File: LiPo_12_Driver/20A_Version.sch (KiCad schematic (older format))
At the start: 47 parts

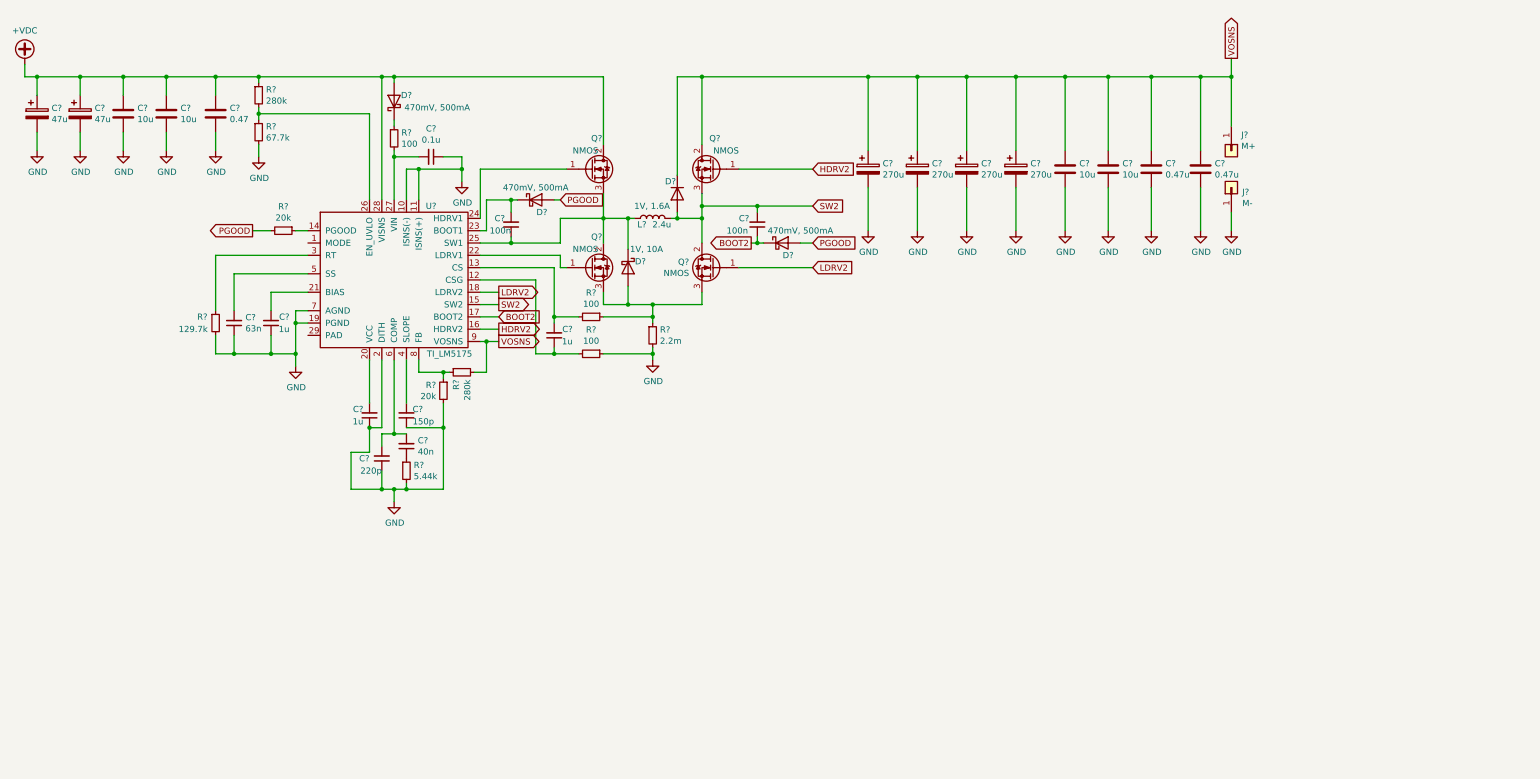
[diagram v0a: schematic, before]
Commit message: Finished LIPO Schematic, started PCB design
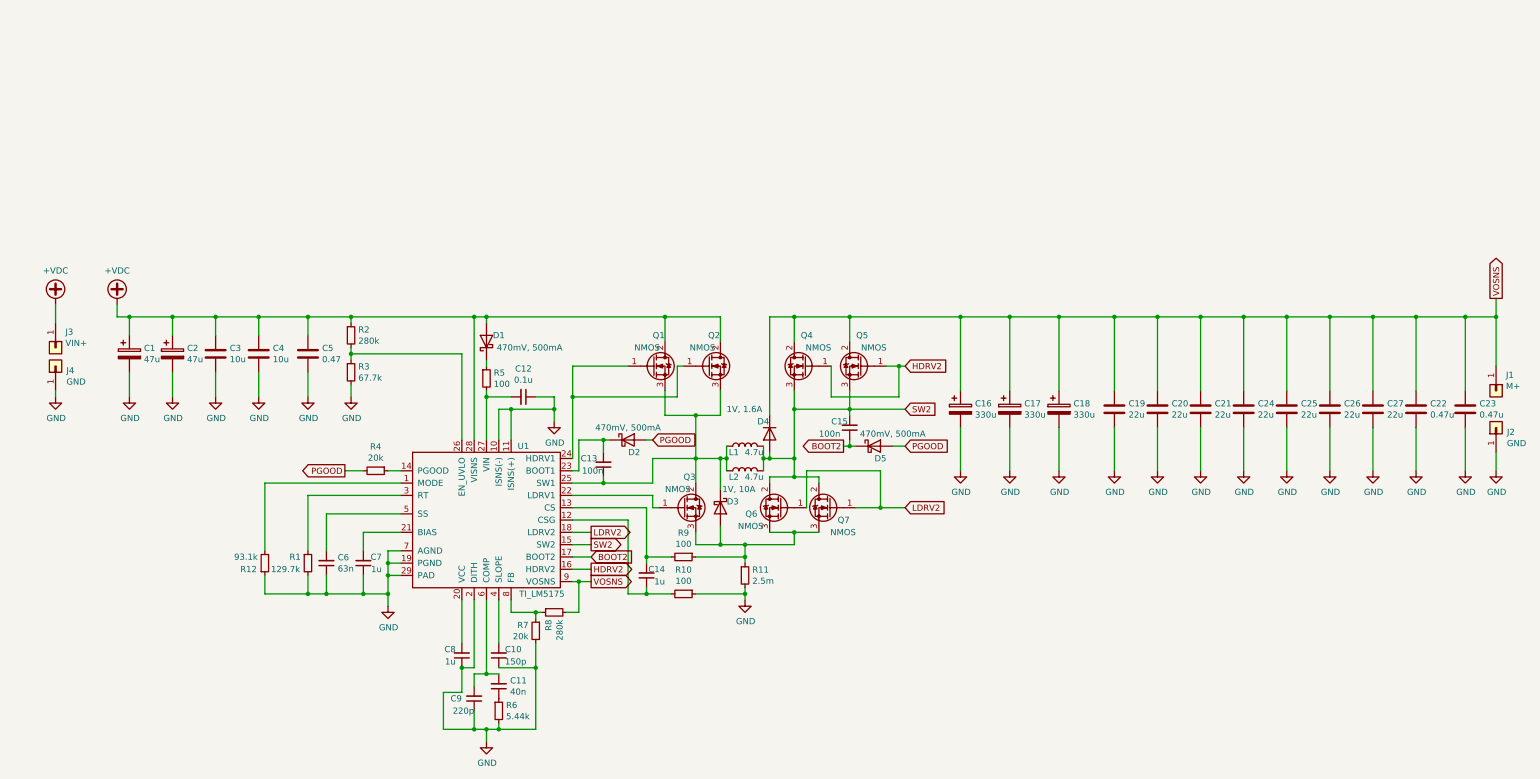
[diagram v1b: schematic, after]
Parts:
- removed C?: 270u, symbol Device:CP
- added C19, C24, C25, C26, C27: 22u, Capacitor_SMD:C_1210_3225Metric_Pad1.42x2.65mm_HandSolder, symbol Device:C
- added J3: VIN+, Connector_PinHeader_2.54mm:PinHeader_1x01_P2.54mm_Vertical, symbol Connector_Generic:Conn_01x01
- added J4: GND, Connector_PinHeader_2.54mm:PinHeader_1x01_P2.54mm_Vertical, symbol Connector_Generic:Conn_01x01
- added L2: 4.7u, Inductor_SMD:L_Vishay_IHLP-6767, symbol Device:L
- added Q2: NMOS, Package_SON:VSONP-8-1EP_5x6_P1.27mm, symbol Device:Q_NMOS_GDS
- added Q4, Q6: NMOS, Package_SON:VSON-8_3.3x3.3mm_P0.65mm_NexFET, symbol Device:Q_NMOS_GDS
- added R12: 93.1k, Resistor_SMD:R_0603_1608Metric_Pad1.05x0.95mm_HandSolder, symbol Device:R_Small
- C1, C2: renamed from C?; footprint (none) -> Capacitor_SMD:CP_Elec_6.3x7.7
- C10, C11, C12, C13, C22, C23, C5, C6, C9: renamed from C?; footprint (none) -> Capacitor_SMD:C_0603_1608Metric_Pad1.05x0.95mm_HandSolder
- C14, C15, C7, C8: renamed from C?; footprint (none) -> Capacitor_SMD:C_0805_2012Metric_Pad1.15x1.40mm_HandSolder
- C16, C17, C18: renamed from C?; value 270u -> 330u; footprint (none) -> Capacitor_SMD:CP_Elec_6.3x9.9
- C20, C21: renamed from C?; value 10u -> 22u; footprint (none) -> Capacitor_SMD:C_1210_3225Metric_Pad1.42x2.65mm_HandSolder
- C3, C4: renamed from C?; footprint (none) -> Capacitor_SMD:C_1210_3225Metric_Pad1.42x2.65mm_HandSolder
- D1, D2, D5: renamed from D?; footprint (none) -> Diode_SMD:D_SOD-123
- D3: renamed from D?; footprint (none) -> Package_TO_SOT_SMD:TO-252-2
- D4: renamed from D?; footprint (none) -> Diode_SMD:D_SMA_Handsoldering
- J1: renamed from J?; footprint (none) -> Connector_PinHeader_2.54mm:PinHeader_1x01_P2.54mm_Vertical
- J2: renamed from J?; value M- -> GND; footprint (none) -> Connector_PinHeader_2.54mm:PinHeader_1x01_P2.54mm_Vertical
- L1: renamed from L?; value 2.4u -> 4.7u; footprint (none) -> Inductor_SMD:L_Vishay_IHLP-6767
- Q1, Q3: renamed from Q?; footprint (none) -> Package_SON:VSONP-8-1EP_5x6_P1.27mm
- Q5, Q7: renamed from Q?; footprint (none) -> Package_SON:VSON-8_3.3x3.3mm_P0.65mm_NexFET
- R1, R2, R3, R6: renamed from R?; footprint (none) -> Resistor_SMD:R_0402_1005Metric
- R10, R4, R5, R7, R8, R9: renamed from R?; footprint (none) -> Resistor_SMD:R_0603_1608Metric_Pad1.05x0.95mm_HandSolder
- R11: renamed from R?; value 2.2m -> 2.5m; footprint (none) -> Resistor_SMD:R_2816_7142Metric_Pad3.20x4.45mm_HandSolder
- U1: renamed from U?; footprint (none) -> Package_DFN_QFN:QFN-28-1EP_4x5mm_P0.5mm_EP2.65x3.65mm_ThermalVias
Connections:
- net +VDC: now also J3.1 (Pin_1), Q2.2 (D)
- net GND: now also U1.29 (PAD), C19.2, C24.2, C25.2, C26.2, C27.2, J4.1 (Pin_1), R12.1
- net HDRV2: now also Q4.1 (G)
- net LDRV2: now also Q6.1 (G)
- net SW2: now also L2.2, Q4.3 (S), Q6.2 (D)
- net VOSNS: now also C19.1, C24.1, C25.1, C26.1, C27.1, Q4.2 (D)
- net at C13.1, D3.1 (K), L1.1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: now also L2.1, Q2.3 (S)
- net at U1.1 (MODE): now also R12.2
- net at Q1.1 (G), U1.24 (HDRV1): now also Q2.1 (G)
- net at D3.2 (A), Q3.3 (S), Q7.3 (S)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: now also Q6.3 (S)
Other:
- moved on the sheet: C1, C10, C11, C12, C13, C14, C15, C16, C17, C18, C2, C20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

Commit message: more lipo pcb dev
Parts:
- removed Q1, Q2, Q3: NMOS, Package_SON:VSONP-8-1EP_5x6_P1.27mm, symbol Device:Q_NMOS_GDS
- removed Q4, Q5, Q6, Q7: NMOS, Package_SON:VSON-8_3.3x3.3mm_P0.65mm_NexFET, symbol Device:Q_NMOS_GDS
- added Q1, Q2, Q3: Q_NMOS, Package_SON:VSONP-8-1EP_5x6_P1.27mm, symbol Device:Q_NMOS_SGD
- added Q4, Q5, Q6, Q7: Q_NMOS, Package_SON:VSON-8_3.3x3.3mm_P0.65mm_NexFET, symbol Device:Q_NMOS_SGD
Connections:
- net +VDC: now also Q1.3 (D), Q2.3 (D)
- net HDRV2: now also Q4.2 (G), Q5.2 (G)
- net LDRV2: now also Q6.2 (G), Q7.2 (G)
- net SW2: now also Q4.1 (S), Q5.1 (S), Q6.3 (D), Q7.3 (D)
- net VOSNS: now also Q4.3 (D), Q5.3 (D)
- net at C13.1, D3.1 (K), L1.1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: now also Q1.1 (S), Q2.1 (S), Q3.3 (D)
- net at U1.22 (LDRV1): now also Q3.2 (G)
- net at U1.24 (HDRV1): now also Q1.2 (G), Q2.2 (G)
- net at D3.2 (A), R11.1, R9.1: now also Q3.1 (S), Q6.1 (S), Q7.1 (S)
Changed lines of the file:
@@
 Wire Wire Line
 	3650 5400 3800 5400
-$Comp
-L Device:Q_NMOS_GDS Q3
-U 1 1 617B6E80
-P 6400 5700
-F 0 "Q3" H 6400 5950 50  0000 L CNN
-F 1 "NMOS" H 6250 5850 50  0000 L CNN
-F 2 "Package_SON:VSONP-8-1EP_5x6_P1.27mm" H 6600 5800 50  0001 C CNN
-F 3 "~" H 6400 5700 50  0001 C CNN
-	1    6400 5700
-	1    0    0    -1
-$EndComp
-$Comp
-L Device:Q_NMOS_GDS Q1
-U 1 1 617B7257
-P 6150 4550
-F 0 "Q1" H 6150 4800 50  0000 L CNN
-F 1 "NMOS" H 6000 4700 50  0000 L CNN
-F 2 "Package_SON:VSONP-8-1EP_5x6_P1.27mm" H 6350 4650 50  0001 C CNN
-F 3 "~" H 6150 4550 50  0001 C CNN
-	1    6150 4550
-	1    0    0    -1
-$EndComp
-$Comp
-L Device:Q_NMOS_GDS Q5
-U 1 1 617B7625
-P 7850 4550
-F 0 "Q5" H 7800 4800 50  0000 L CNN
-F 1 "NMOS" H 7650 4700 50  0000 L CNN
-F 2 "Package_SON:VSON-8_3.3x3.3mm_P0.65mm_NexFET" H 8050 4650 50  0001 C CNN
-F 3 "~" H 7850 4550 50  0001 C CNN
-	1    7850 4550
-	-1   0    0    -1
-$EndComp
-$Comp
-L Device:Q_NMOS_GDS Q7
-U 1 1 617B7A51
-P 7600 5700
-F 0 "Q7" H 7450 5600 50  0000 L CNN
-F 1 "NMOS" H 7400 5500 50  0000 L CNN
-F 2 "Package_SON:VSON-8_3.3x3.3mm_P0.65mm_NexFET" H 7800 5800 50  0001 C CNN
-F 3 "~" H 7600 5700 50  0001 C CNN
-	1    7600 5700
-	-1   0    0    -1
-$EndComp
 Wire Wire Line
 	6750 5300 6700 5300
@@
 Wire Wire Line
 	6250 4950 6250 4750
-$Comp
-L Device:Q_NMOS_GDS Q2
-U 1 1 618E7504
+Wire Wire Line
+	6700 4750 6700 4950
+Wire Wire Line
+	6700 4950 6500 4950
+Connection ~ 6500 4950
+Wire Wire Line
+	6700 4350 6700 4150
+Wire Wire Line
+	6700 4150 6250 4150
+Connection ~ 6250 4150
+Wire Wire Line
+	5500 4800 6350 4800
+Wire Wire Line
+	6350 4800 6350 4550
+Wire Wire Line
+	6350 4550 6400 4550
+Connection ~ 5500 4800
+Wire Wire Line
+	5500 4800 5500 4550
+Wire Wire Line
+	7300 4900 7300 5300
+Wire Wire Line
+	7100 5300 7300 5300
+Connection ~ 7100 5300
+Connection ~ 7300 5300
+Wire Wire Line
+	7300 5300 7300 5450
+Wire Wire Line
+	7800 5700 8000 5700
+Wire Wire Line
+	7500 5900 7300 5900
+Wire Wire Line
+	7100 5900 7300 5900
+Connection ~ 7300 5900
+Wire Wire Line
+	7100 5500 7100 5450
+Wire Wire Line
+	7100 5450 7300 5450
+Connection ~ 7300 5450
+Wire Wire Line
+	7500 5500 7500 5450
+Wire Wire Line
+	7500 5450 7300 5450
+Wire Wire Line
+	8000 5700 8000 5400
+Wire Wire Line
+	8000 5400 7400 5400
+Wire Wire Line
+	7400 5400 7400 5700
+Connection ~ 8000 5700
+Wire Wire Line
+	8000 5700 8200 5700
+Wire Wire Line
+	7750 4150 7750 4350
+Connection ~ 7750 4150
+Wire Wire Line
+	7750 4150 8650 4150
+Wire Wire Line
+	7750 4750 7750 4900
+Wire Wire Line
+	8050 4550 8150 4550
+Wire Wire Line
+	8150 4550 8150 4800
+Wire Wire Line
+	8150 4800 7600 4800
+Wire Wire Line
+	7600 4800 7600 4550
+Connection ~ 8150 4550
+Wire Wire Line
+	8150 4550 8200 4550
+$Comp
+L Device:Q_NMOS_SGD Q1
+U 1 1 617B93BB
+P 6150 4550
+F 0 "Q1" H 6100 4800 50  0000 L CNN
+F 1 "Q_NMOS" H 5900 4700 50  0000 L CNN
+F 2 "Package_SON:VSONP-8-1EP_5x6_P1.27mm" H 6350 4650 50  0001 C CNN
+F 3 "~" H 6150 4550 50  0001 C CNN
+	1    6150 4550
+	1    0    0    -1
+$EndComp
+$Comp
+L Device:Q_NMOS_SGD Q2
+U 1 1 617BFAC8
 P 6600 4550
 F 0 "Q2" H 6600 4800 50  0000 L CNN
-F 1 "NMOS" H 6450 4700 50  0000 L CNN
+F 1 "Q_NMOS" H 6350 4700 50  0000 L CNN
 F 2 "Package_SON:VSONP-8-1EP_5x6_P1.27mm" H 6800 4650 50  0001 C CNN
 F 3 "~" H 6600 4550 50  0001 C CNN
@@
 	1    0    0    -1
 $EndComp
-Wire Wire Line
-	6700 4750 6700 4950
-Wire Wire Line
-	6700 4950 6500 4950
-Connection ~ 6500 4950
-Wire Wire Line
-	6700 4350 6700 4150
-Wire Wire Line
-	6700 4150 6250 4150
-Connection ~ 6250 4150
-Wire Wire Line
-	5500 4800 6350 4800
-Wire Wire Line
-	6350 4800 6350 4550
-Wire Wire Line
-	6350 4550 6400 4550
-Connection ~ 5500 4800
-Wire Wire Line
-	5500 4800 5500 4550
-Wire Wire Line
-	7300 4900 7300 5300
-Wire Wire Line
-	7100 5300 7300 5300
-Connection ~ 7100 5300
-Connection ~ 7300 5300
-Wire Wire Line
-	7300 5300 7300 5450
-$Comp
-L Device:Q_NMOS_GDS Q6
-U 1 1 61939310
+$Comp
+L Device:Q_NMOS_SGD Q3
+U 1 1 617C90DC
+P 6400 5700
+F 0 "Q3" H 6400 5950 50  0000 L CNN
+F 1 "Q_NMOS" H 6150 5850 50  0000 L CNN
+F 2 "Package_SON:VSONP-8-1EP_5x6_P1.27mm" H 6600 5800 50  0001 C CNN
+F 3 "~" H 6400 5700 50  0001 C CNN
+	1    6400 5700
+	1    0    0    -1
+$EndComp
+$Comp
+L Device:Q_NMOS_SGD Q4
+U 1 1 617CFEE4
+P 7400 4550
+F 0 "Q4" H 7400 4800 50  0000 L CNN
+F 1 "Q_NMOS" H 7100 4700 50  0000 L CNN
+F 2 "Package_SON:VSON-8_3.3x3.3mm_P0.65mm_NexFET" H 7600 4650 50  0001 C CNN
+F 3 "~" H 7400 4550 50  0001 C CNN
+	1    7400 4550
+	-1   0    0    -1
+$EndComp
+$Comp
+L Device:Q_NMOS_SGD Q5
+U 1 1 617D5AFF
+P 7850 4550
+F 0 "Q5" H 7850 4800 50  0000 L CNN
+F 1 "Q_NMOS" H 7550 4700 50  0000 L CNN
+F 2 "Package_SON:VSON-8_3.3x3.3mm_P0.65mm_NexFET" H 8050 4650 50  0001 C CNN
+F 3 "~" H 7850 4550 50  0001 C CNN
+	1    7850 4550
+	-1   0    0    -1
+$EndComp
+$Comp
+L Device:Q_NMOS_SGD Q6
+U 1 1 617D7412
 P 7200 5700
-F 0 "Q6" H 7400 5650 50  0000 L CNN
-F 1 "NMOS" H 7350 5550 50  0000 L CNN
+F 0 "Q6" H 7050 5750 50  0000 L CNN
+F 1 "Q_NMOS" H 6950 5900 50  0000 L CNN
 F 2 "Package_SON:VSON-8_3.3x3.3mm_P0.65mm_NexFET" H 7400 5800 50  0001 C CNN
 F 3 "~" H 7200 5700 50  0001 C CNN
@@
 	-1   0    0    -1
 $EndComp
-Wire Wire Line
-	7800 5700 8000 5700
-Wire Wire Line
-	7500 5900 7300 5900
-Wire Wire Line
-	7100 5900 7300 5900
-Connection ~ 7300 5900
-Wire Wire Line
-	7100 5500 7100 5450
-Wire Wire Line
-	7100 5450 7300 5450
-Connection ~ 7300 5450
-Wire Wire Line
-	7500 5500 7500 5450
-Wire Wire Line
-	7500 5450 7300 5450
-Wire Wire Line
-	8000 5700 8000 5400
-Wire Wire Line
-	8000 5400 7400 5400
-Wire Wire Line
-	7400 5400 7400 5700
-Connection ~ 8000 5700
-Wire Wire Line
-	8000 5700 8200 5700
-$Comp
-L Device:Q_NMOS_GDS Q4
-U 1 1 61982AE0
-P 7400 4550
-F 0 "Q4" H 7350 4800 50  0000 L CNN
-F 1 "NMOS" H 7200 4700 50  0000 L CNN
-F 2 "Package_SON:VSON-8_3.3x3.3mm_P0.65mm_NexFET" H 7600 4650 50  0001 C CNN
-F 3 "~" H 7400 4550 50  0001 C CNN
-	1    7400 4550
+$Comp
+L Device:Q_NMOS_SGD Q7
+U 1 1 617D87B0
+P 7600 5700
+F 0 "Q7" H 7500 5850 50  0000 L CNN
+F 1 "Q_NMOS" H 7250 5750 50  0000 L CNN
+F 2 "Package_SON:VSON-8_3.3x3.3mm_P0.65mm_NexFET" H 7800 5800 50  0001 C CNN
+F 3 "~" H 7600 5700 50  0001 C CNN
+	1    7600 5700
 	-1   0    0    -1
 $EndComp
-Wire Wire Line
-	7750 4150 7750 4350
-Connection ~ 7750 4150
-Wire Wire Line
-	7750 4150 8650 4150
-Wire Wire Line
-	7750 4750 7750 4900
-Wire Wire Line
-	8050 4550 8150 4550
-Wire Wire Line
-	8150 4550 8150 4800
-Wire Wire Line
-	8150 4800 7600 4800
-Wire Wire Line
-	7600 4800 7600 4550
-Connection ~ 8150 4550
-Wire Wire Line
-	8150 4550 8200 4550
 $EndSCHEMATC

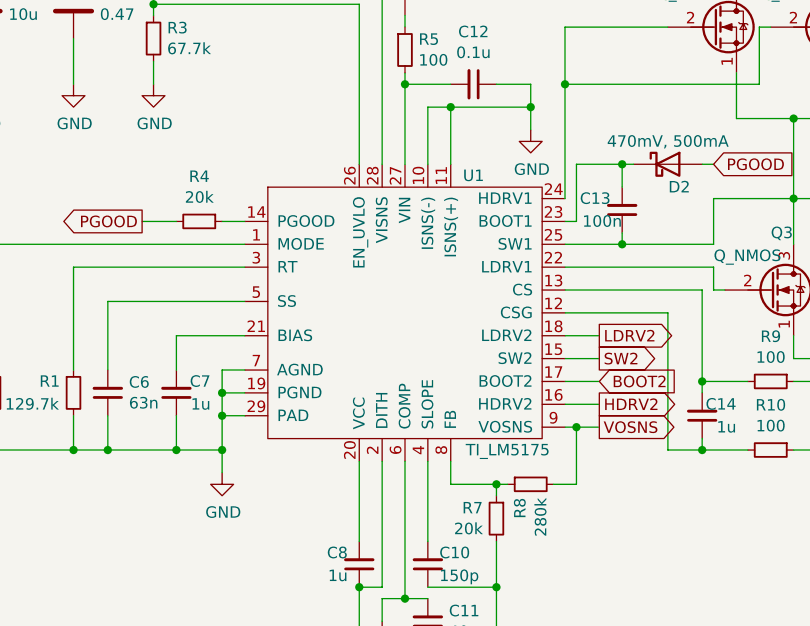
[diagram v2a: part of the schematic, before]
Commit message: Updated PCB because QFN package is out of stockaslhdflsakghlksa
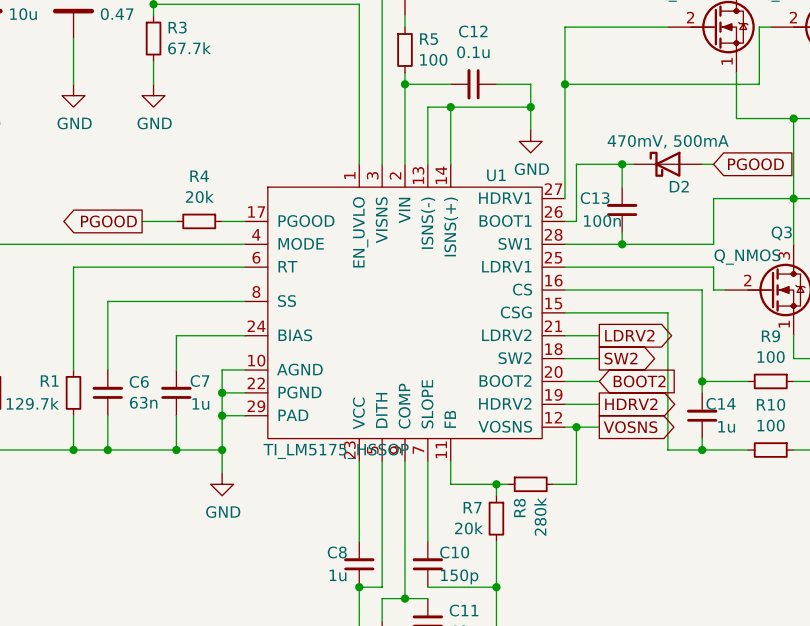
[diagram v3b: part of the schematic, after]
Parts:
- removed U1: TI_LM5175, Package_DFN_QFN:QFN-28-1EP_4x5mm_P0.5mm_EP2.65x3.65mm_ThermalVias, symbol LiPo_12_Driver:TI_LM5175
- added U1: TI_LM5175_HSSOP, Package_SO:HTSSOP-28-1EP_4.4x9.7mm_P0.65mm_EP3.4x9.5mm_ThermalVias, symbol LiPo_12_Driver:TI_LM5175_HSSOP
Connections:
- net +VDC: now also U1.3 (VISNS)
- net BOOT2: now also U1.20 (BOOT2)
- net GND: now also U1.10 (AGND), U1.13 (ISNS(-)), U1.14 (ISNS(+)), U1.22 (PGND), U1.29 (PAD), U1.5 (DITH)
- net HDRV2: now also U1.19 (HDRV2)
- net LDRV2: now also U1.21 (LDRV2)
- net SW2: now also U1.18 (SW2)
- net VOSNS: now also U1.12 (VOSNS)
- net at C13.1, D3.1 (K), L1.1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: now also U1.28 (SW1)
- net at R12.2: now also U1.4 (MODE)
- net at C14.1, R10.2: now also U1.15 (CSG)
- net at C14.2, R9.2: now also U1.16 (CS)
- net at R4.1: now also U1.17 (PGOOD)
- net at C8.2: now also U1.23 (VCC)
- net at C7.2: now also U1.24 (BIAS)
- net at Q3.2 (G): now also U1.25 (LDRV1)
- net at C13.2, D2.1 (K): now also U1.26 (BOOT1)
- net at Q1.2 (G), Q2.2 (G): now also U1.27 (HDRV1)
- net at R2.2, R3.1: now also U1.1 (EN_UVLO)
- net at C12.2, R5.2: now also U1.2 (VIN)
- net at R1.1: now also U1.6 (RT)
- net at C10.2: now also U1.7 (SLOPE)
- net at C6.2: now also U1.8 (SS)
- net at C11.2, C9.2: now also U1.9 (COMP)
- net at R7.1, R8.1: now also U1.11 (FB)
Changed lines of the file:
@@
 Wire Wire Line
 	3500 6400 3800 6400
-$Comp
-L LiPo_12_Driver:TI_LM5175 U1
-U 1 1 616B56F3
-P 4650 5600
-F 0 "U1" H 5100 6000 50  0000 C CNN
-F 1 "TI_LM5175" H 5250 4800 50  0000 C CNN
-F 2 "Package_DFN_QFN:QFN-28-1EP_4x5mm_P0.5mm_EP2.65x3.65mm_ThermalVias" H 4650 5600 50  0001 C CNN
-F 3 "" H 4650 5600 50  0001 C CNN
-	1    4650 5600
-	1    0    0    -1
-$EndComp
 Wire Wire Line
 	4100 6150 4000 6150
@@
 Wire Wire Line
 	2950 4150 3350 4150
-Wire Wire Line
-	3800 5900 4100 5900
 $Comp
 L Device:R_Small R4
@@
 	4000 6250 4000 6150
 Wire Wire Line
-	3000 5500 4100 5500
-Wire Wire Line
 	3000 6250 3000 6400
 $Comp
@@
 	-1   0    0    -1
 $EndComp
+Wire Wire Line
+	3800 5900 4100 5900
+Wire Wire Line
+	3000 5500 4100 5500
+$Comp
+L LiPo_12_Driver:TI_LM5175_HSSOP U1
+U 1 1 6181A349
+P 4800 5800
+F 0 "U1" H 5200 6400 50  0000 C CNN
+F 1 "TI_LM5175_HSSOP" H 4500 5200 50  0000 C CNN
+F 2 "Package_SO:HTSSOP-28-1EP_4.4x9.7mm_P0.65mm_EP3.4x9.5mm_ThermalVias" H 4800 5800 50  0001 C CNN
+F 3 "" H 4800 5800 50  0001 C CNN
+	1    4800 5800
+	1    0    0    -1
+$EndComp
 $EndSCHEMATC

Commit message: updated some stuff
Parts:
- C11: value 40n -> 47n
- C14: value 1u -> 47p
- C6: value 63n -> 68n
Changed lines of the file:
@@
 P 4900 7150
 F 0 "C11" H 4808 7104 50  0000 R CNN
-F 1 "40n" H 4808 7195 50  0000 R CNN
+F 1 "47n" H 4808 7195 50  0000 R CNN
 F 2 "Capacitor_SMD:C_0603_1608Metric_Pad1.05x0.95mm_HandSolder" H 4900 7150 50  0001 C CNN
 F 3 "~" H 4900 7150 50  0001 C CNN
@@
 P 3500 6150
 F 0 "C6" H 3408 6104 50  0000 R CNN
-F 1 "63n" H 3408 6195 50  0000 R CNN
+F 1 "68n" H 3408 6195 50  0000 R CNN
 F 2 "Capacitor_SMD:C_0603_1608Metric_Pad1.05x0.95mm_HandSolder" H 3500 6150 50  0001 C CNN
 F 3 "~" H 3500 6150 50  0001 C CNN
@@
 P 6100 6250
 F 0 "C14" H 6250 6200 50  0000 R CNN
-F 1 "1u" H 6250 6300 50  0000 R CNN
+F 1 "47p" H 6250 6300 50  0000 R CNN
 F 2 "Capacitor_SMD:C_0805_2012Metric_Pad1.15x1.40mm_HandSolder" H 6100 6250 50  0001 C CNN
 F 3 "~" H 6100 6250 50  0001 C CNN
